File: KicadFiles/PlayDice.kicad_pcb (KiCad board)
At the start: 2 copper layers, 40 x 110 mm, 31 parts, among them J1 Clock In, J2 Eurorack_10_pin_power, J3 Action In, J4 OLED, J5 Gate Out, J6 CV Out, Q1 2N3904, Q2 2N3904, U1 LM1117-5.0, U3 TL072

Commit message: PCB fixed transistor connections; added basic handling for scale quantisation
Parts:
- Q1, Q2: value 2N3904 -> MMBT3904
- moved R4 7.02 mm to (131.0, 122.0), turned to 270 degrees
- moved Q2 5.59 mm to (137.5, 119.0)
- moved R3 3.04 mm to (135.0, 123.5)
- moved Q1 1.58 mm to (116.0, 145.5), turned to 180 degrees
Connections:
- Q1 pad 1: GND -> Net-(Q1-Pad1)
- Q1 pad 2: Net-(Q1-Pad2) -> GND
- Q2 pad 1: GND -> Net-(Q2-Pad1)
- Q2 pad 2: Net-(Q2-Pad2) -> GND
- R1 pad 1: Net-(Q1-Pad2) -> Net-(Q1-Pad1)
- R2 pad 1: Net-(Q1-Pad2) -> Net-(Q1-Pad1)
- R3 pad 1: Net-(Q2-Pad2) -> Net-(Q2-Pad1)
- R4 pad 1: Net-(Q2-Pad2) -> Net-(Q2-Pad1)
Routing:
- net Net-(Q1-Pad2): track 18.1 -> 0.00 mm
- net Net-(Q1-Pad1): track 0.00 -> 17.5 mm
- net Net-(Q2-Pad1): track 0.00 -> 9.81 mm
- net Net-(Q2-Pad2): track 5.59 -> 0.00 mm
- net /ACTIONCV: track 54.8 -> 51.5 mm
- net Net-(J3-Pad3): track 5.39 -> 3.22 mm
- net /CLOCK: track 84.5 -> 83.7 mm
- net (no net): track 0.00 -> 0.50 mm

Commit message: Bug Fixes and panel updates
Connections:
- Action1 pad 1: GND -> (no net)
- Action1 pad 3: (no net) -> GND
- Lane1 pad 1: GND -> (no net)
- Lane1 pad 3: (no net) -> GND
- Left1 pad 1: GND -> (no net)
- Left1 pad 3: (no net) -> GND
- Right1 pad 1: GND -> (no net)
- Right1 pad 3: (no net) -> GND
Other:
- board text added: "CV Out"
- board text added: "Clock In"
- board text added: "Gate Out"
- board text added: "Play Dice v 0.3"
- board text added: "RED -12"
- board text removed: "-12"
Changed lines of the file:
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@@
     (area 102.924999 48.924999 143.075001 159.075001)
     (thickness 1.6)
-    (drawings 7)
+    (drawings 14)
     (tracks 184)
     (zones 0)
@@
     (44 Edge.Cuts user)
     (45 Margin user)
-    (46 B.CrtYd user)
+    (46 B.CrtYd user hide)
     (47 F.CrtYd user)
-    (48 B.Fab user)
-    (49 F.Fab user)
+    (48 B.Fab user hide)
+    (49 F.Fab user hide)
   )
   (setup
@@
     (descr http://www.farnell.com/datasheets/1520732.pdf)
     (tags "connector multicomp MC9A MC9A12")
-    (fp_text reference J2 (at -3 -7 90) (layer F.SilkS) hide
+    (fp_text reference J2 (at 5 -7 90) (layer F.SilkS) hide
       (effects (font (size 1 1) (thickness 0.15)))
     )
@@
     (fp_line (start 8.8 -0.8) (end 8.8 -10.8) (layer B.Fab) (width 0.1))
     (fp_line (start 8.8 -10.8) (end -1.2 -10.8) (layer B.Fab) (width 0.1))
-    (pad 3 thru_hole circle (at 7.6 0 270) (size 1.8 1.8) (drill 0.9) (layers *.Cu *.Mask))
+    (pad 3 thru_hole circle (at 7.6 0 270) (size 1.8 1.8) (drill 0.9) (layers *.Cu *.Mask)
+      (net 2 GND))
     (pad 4 thru_hole circle (at 7.6 -11.6 270) (size 1.8 1.8) (drill 0.9) (layers *.Cu *.Mask))
-    (pad 1 thru_hole rect (at 0 0 270) (size 1.8 1.8) (drill 0.9) (layers *.Cu *.Mask)
-      (net 2 GND))
+    (pad 1 thru_hole rect (at 0 0 270) (size 1.8 1.8) (drill 0.9) (layers *.Cu *.Mask))
     (pad 2 thru_hole circle (at 0 -11.6 270) (size 1.8 1.8) (drill 0.9) (layers *.Cu *.Mask)
       (net 3 /ACTION))
@@
     (fp_line (start 8.8 -0.8) (end 8.8 -10.8) (layer B.Fab) (width 0.1))
     (fp_line (start 8.8 -10.8) (end -1.2 -10.8) (layer B.Fab) (width 0.1))
-    (pad 3 thru_hole circle (at 7.6 0 270) (size 1.8 1.8) (drill 0.9) (layers *.Cu *.Mask))
+    (pad 3 thru_hole circle (at 7.6 0 270) (size 1.8 1.8) (drill 0.9) (layers *.Cu *.Mask)
+      (net 2 GND))
     (pad 4 thru_hole circle (at 7.6 -11.6 270) (size 1.8 1.8) (drill 0.9) (layers *.Cu *.Mask))
-    (pad 1 thru_hole rect (at 0 0 270) (size 1.8 1.8) (drill 0.9) (layers *.Cu *.Mask)
-      (net 2 GND))
+    (pad 1 thru_hole rect (at 0 0 270) (size 1.8 1.8) (drill 0.9) (layers *.Cu *.Mask))
     (pad 2 thru_hole circle (at 0 -11.6 270) (size 1.8 1.8) (drill 0.9) (layers *.Cu *.Mask)
       (net 32 /LANE))
@@
     (fp_line (start 8.8 -0.8) (end 8.8 -10.8) (layer B.Fab) (width 0.1))
     (fp_line (start 8.8 -10.8) (end -1.2 -10.8) (layer B.Fab) (width 0.1))
-    (pad 3 thru_hole circle (at 7.6 0 270) (size 1.8 1.8) (drill 0.9) (layers *.Cu *.Mask))
+    (pad 3 thru_hole circle (at 7.6 0 270) (size 1.8 1.8) (drill 0.9) (layers *.Cu *.Mask)
+      (net 2 GND))
     (pad 4 thru_hole circle (at 7.6 -11.6 270) (size 1.8 1.8) (drill 0.9) (layers *.Cu *.Mask))
-    (pad 1 thru_hole rect (at 0 0 270) (size 1.8 1.8) (drill 0.9) (layers *.Cu *.Mask)
-      (net 2 GND))
+    (pad 1 thru_hole rect (at 0 0 270) (size 1.8 1.8) (drill 0.9) (layers *.Cu *.Mask))
     (pad 2 thru_hole circle (at 0 -11.6 270) (size 1.8 1.8) (drill 0.9) (layers *.Cu *.Mask)
       (net 33 /RIGHT))
@@
     (fp_line (start 8.8 -0.8) (end 8.8 -10.8) (layer B.Fab) (width 0.1))
     (fp_line (start 8.8 -10.8) (end -1.2 -10.8) (layer B.Fab) (width 0.1))
-    (pad 3 thru_hole circle (at 7.6 0 270) (size 1.8 1.8) (drill 0.9) (layers *.Cu *.Mask))
+    (pad 3 thru_hole circle (at 7.6 0 270) (size 1.8 1.8) (drill 0.9) (layers *.Cu *.Mask)
+      (net 2 GND))
     (pad 4 thru_hole circle (at 7.6 -11.6 270) (size 1.8 1.8) (drill 0.9) (layers *.Cu *.Mask))
-    (pad 1 thru_hole rect (at 0 0 270) (size 1.8 1.8) (drill 0.9) (layers *.Cu *.Mask)
-      (net 2 GND))
+    (pad 1 thru_hole rect (at 0 0 270) (size 1.8 1.8) (drill 0.9) (layers *.Cu *.Mask))
     (pad 2 thru_hole circle (at 0 -11.6 270) (size 1.8 1.8) (drill 0.9) (layers *.Cu *.Mask)
       (net 34 /LEFT))
@@
     (tags "resistor 0805")
     (attr smd)
-    (fp_text reference R7 (at -2.5 -2 180) (layer F.SilkS)
+    (fp_text reference R7 (at -1.5 -1.5 270) (layer F.SilkS)
       (effects (font (size 1 1) (thickness 0.15)))
     )
@@
     (tags "capacitor 0805")
     (attr smd)
-    (fp_text reference C4 (at -2.5 2 180) (layer F.SilkS)
+    (fp_text reference C4 (at 0 1.5 270) (layer F.SilkS)
       (effects (font (size 1 1) (thickness 0.15)))
     )
@@
     (pad "" np_thru_hole circle (at 0 0 180) (size 2.5 2.5) (drill 2.5) (layers *.Cu *.Mask))
   )
+  (gr_text "CV Out" (at 110 147.5) (layer F.SilkS)
+    (effects (font (size 1 1) (thickness 0.1)))
+  )
+  (gr_text "Gate Out" (at 123 147.5) (layer F.SilkS)
+    (effects (font (size 1 1) (thickness 0.1)))
+  )
+  (gr_text "Clock In" (at 136 147.5) (layer F.SilkS)
+    (effects (font (size 1 1) (thickness 0.1)))
+  )
+  (gr_line (start 120.5 113.25) (end 125.5 113.25) (angle 90) (layer F.SilkS) (width 0.2))
+  (gr_line (start 123 118.5) (end 123 117.5) (angle 90) (layer F.SilkS) (width 0.2))
+  (gr_line (start 123 113.5) (end 123 118) (angle 90) (layer F.SilkS) (width 0.2))
+  (gr_text "Play Dice\nv 0.3" (at 109 52.5) (layer F.SilkS)
+    (effects (font (size 1.2 1.2) (thickness 0.3)))
+  )
   (gr_circle (center 117 115) (end 117.5 115) (layer F.SilkS) (width 0.2))
   (gr_text +12 (at 122.5 122.5) (layer F.SilkS)
     (effects (font (size 1 1) (thickness 0.15)))
   )
-  (gr_text -12 (at 121.5 137.5) (layer F.SilkS)
+  (gr_text "RED\n-12" (at 129.5 135) (layer F.SilkS)
     (effects (font (size 1 1) (thickness 0.15)))
   )

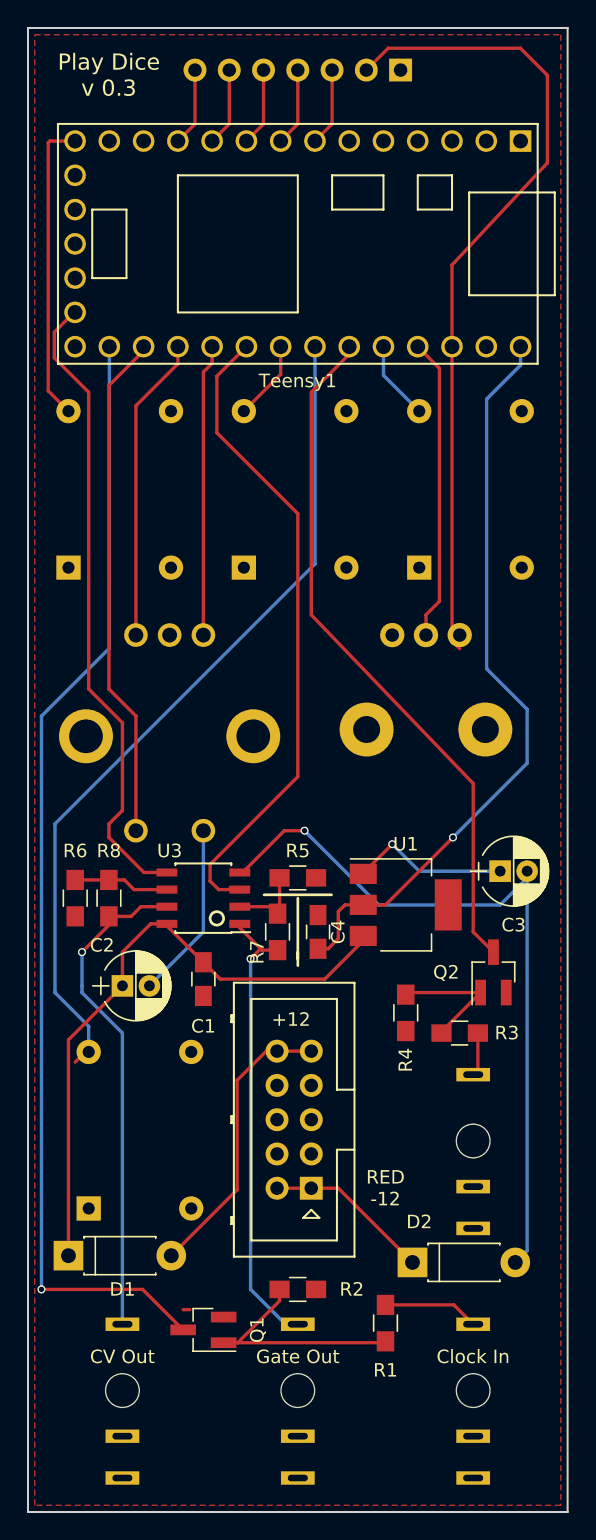
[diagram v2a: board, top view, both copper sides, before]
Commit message: Various code tidy-ups. Added configuration option for encoder direction. ADded new panel gerbers
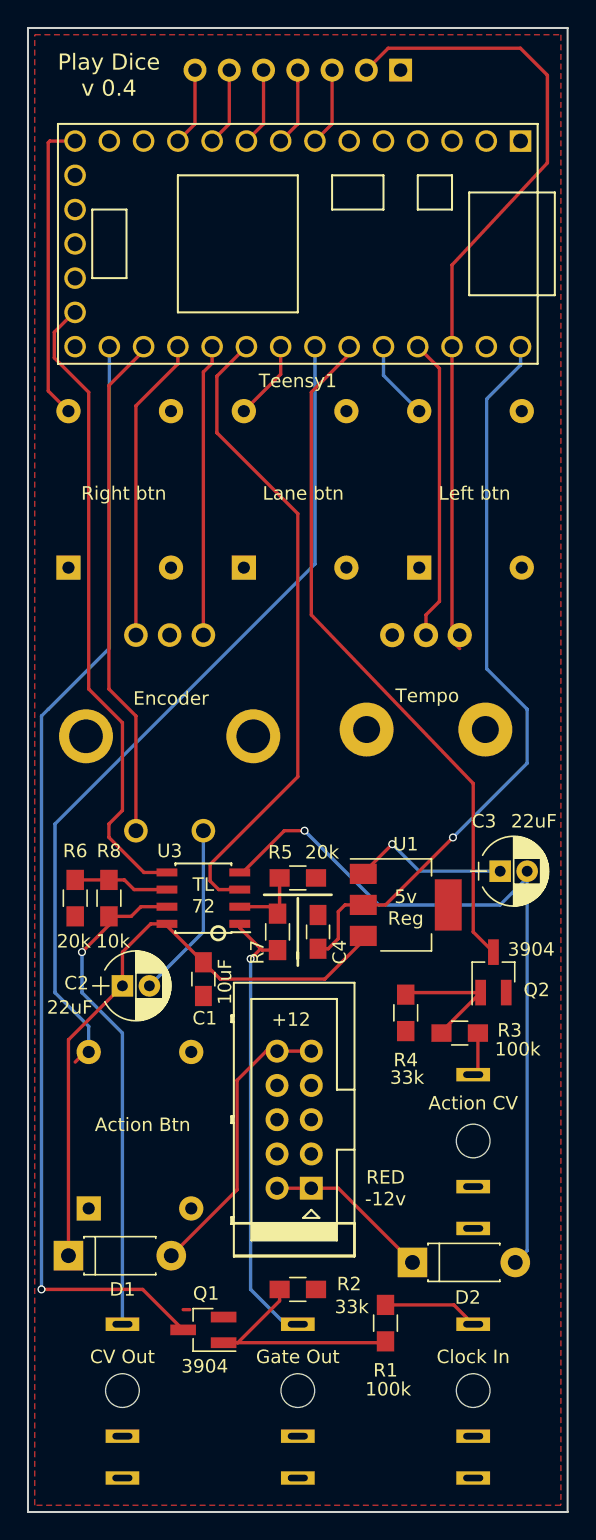
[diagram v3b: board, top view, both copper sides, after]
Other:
- board text added: "100k"
- board text added: "10k"
- board text added: "10uF"
- board text added: "20k"
- board text added: "22uF"
- board text added: "33k"
- board text added: "3904"
- board text added: "5v Reg"
- board text added: "Action Btn"
- board text added: "Action CV"
- board text added: "Encoder"
- board text added: "Lane btn"
- board text added: "Left btn"
- board text added: "Play Dice v 0.4"
- board text added: "RED -12v"
- board text added: "Right btn"
- board text added: "TL 72"
- board text added: "Tempo"
- board text removed: "Play Dice v 0.3"
- board text removed: "RED -12"
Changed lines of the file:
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@@
     (links 75)
     (no_connects 0)
-    (area 102.924999 48.924999 143.075001 159.075001)
+    (area 102.924999 44.05 143.075001 159.075001)
     (thickness 1.6)
-    (drawings 14)
+    (drawings 38)
     (tracks 184)
     (zones 0)
@@
       (drillshape 0)
       (scaleselection 1)
-      (outputdirectory Gerbers/))
+      (outputdirectory "Board Gerbers/"))
   )
   (net 0 "")
@@
     (descr "D, DO-41_SOD81 series, Axial, Horizontal, pin pitch=7.62mm, , length*diameter=5.2*2.7mm^2, , http://www.diodes.com/_files/packages/DO-41%20(Plastic).pdf")
     (tags "D DO-41_SOD81 series Axial Horizontal pin pitch 7.62mm  length 5.2mm diameter 2.7mm")
-    (fp_text reference D2 (at 0.5 -3) (layer F.SilkS)
+    (fp_text reference D2 (at 4.1 2.6) (layer F.SilkS)
       (effects (font (size 1 1) (thickness 0.15)))
     )
@@
     (descr "CP, Radial series, Radial, pin pitch=2.00mm, , diameter=5mm, Electrolytic Capacitor")
     (tags "CP Radial series Radial pin pitch 2.00mm  diameter 5mm Electrolytic Capacitor")
-    (fp_text reference C3 (at 1 4) (layer F.SilkS)
+    (fp_text reference C3 (at -1.2 -3.7) (layer F.SilkS)
       (effects (font (size 1 1) (thickness 0.15)))
     )
@@
     (descr "CP, Radial series, Radial, pin pitch=2.00mm, , diameter=5mm, Electrolytic Capacitor")
     (tags "CP Radial series Radial pin pitch 2.00mm  diameter 5mm Electrolytic Capacitor")
-    (fp_text reference C2 (at -1.5 -3 180) (layer F.SilkS)
+    (fp_text reference C2 (at -3.4 -0.2 180) (layer F.SilkS)
       (effects (font (size 1 1) (thickness 0.15)))
     )
@@
     (tags "resistor 0805")
     (attr smd)
-    (fp_text reference R2 (at 4 0) (layer F.SilkS)
+    (fp_text reference R2 (at 3.8 -0.4) (layer F.SilkS)
       (effects (font (size 1 1) (thickness 0.15)))
     )
@@
     (tags "resistor 0805")
     (attr smd)
-    (fp_text reference R3 (at 3.5 0) (layer F.SilkS)
+    (fp_text reference R3 (at 3.7 -0.2) (layer F.SilkS)
       (effects (font (size 1 1) (thickness 0.15)))
     )
@@
     (tags "resistor 0805")
     (attr smd)
-    (fp_text reference R4 (at 3.5 0 270) (layer F.SilkS)
+    (fp_text reference R4 (at 3.5 0 360) (layer F.SilkS)
       (effects (font (size 1 1) (thickness 0.15)))
     )
@@
     (tags "resistor 0805")
     (attr smd)
-    (fp_text reference R5 (at 0 2 180) (layer F.SilkS)
+    (fp_text reference R5 (at 1.3 1.9 180) (layer F.SilkS)
       (effects (font (size 1 1) (thickness 0.15)))
     )
@@
     (tags SOT-23)
     (attr smd)
-    (fp_text reference Q1 (at -4 0 270) (layer F.SilkS)
+    (fp_text reference Q1 (at -0.2 2.7 180) (layer F.SilkS)
       (effects (font (size 1 1) (thickness 0.15)))
     )
@@
     (tags SOT-23)
     (attr smd)
-    (fp_text reference Q2 (at 0 -3.5 180) (layer F.SilkS)
+    (fp_text reference Q2 (at -1.3 3.2 180) (layer F.SilkS)
       (effects (font (size 1 1) (thickness 0.15)))
     )
@@
     (tags "capacitor 0805")
     (attr smd)
-    (fp_text reference C1 (at 3.5 0 360) (layer F.SilkS)
+    (fp_text reference C1 (at 2.9 -0.1 360) (layer F.SilkS)
       (effects (font (size 1 1) (thickness 0.15)))
     )
@@
     (tags "capacitor 0805")
     (attr smd)
-    (fp_text reference C4 (at 0 1.5 270) (layer F.SilkS)
+    (fp_text reference C4 (at -1.5 1.6 270) (layer F.SilkS)
       (effects (font (size 1 1) (thickness 0.15)))
     )
@@
     (pad "" np_thru_hole circle (at 0 0 180) (size 2.5 2.5) (drill 2.5) (layers *.Cu *.Mask))
   )
+  (gr_text 10uF (at 117.6 119.7 90) (layer F.SilkS)
+    (effects (font (size 1 1) (thickness 0.1)))
+  )
+  (gr_text 22uF (at 140.5 107.8) (layer F.SilkS)
+    (effects (font (size 1 1) (thickness 0.1)))
+  )
+  (gr_text 22uF (at 106.1 121.6) (layer F.SilkS)
+    (effects (font (size 1 1) (thickness 0.1)))
+  )
+  (gr_text 3904 (at 116.1 148.2) (layer F.SilkS)
+    (effects (font (size 1 1) (thickness 0.1)))
+  )
+  (gr_text 3904 (at 140.3 117.3) (layer F.SilkS)
+    (effects (font (size 1 1) (thickness 0.1)))
+  )
+  (gr_text "5v\nReg" (at 131 114.2) (layer F.SilkS)
+    (effects (font (size 1 1) (thickness 0.1)))
+  )
+  (gr_text "TL\n72" (at 116 113.3) (layer F.SilkS)
+    (effects (font (size 1 1) (thickness 0.1)))
+  )
+  (gr_text 10k (at 109.3 116.7) (layer F.SilkS)
+    (effects (font (size 1 1) (thickness 0.1)))
+  )
+  (gr_text 20k (at 106.4 116.7) (layer F.SilkS)
+    (effects (font (size 1 1) (thickness 0.1)))
+  )
+  (gr_text 20k (at 124.8 110.1) (layer F.SilkS)
+    (effects (font (size 1 1) (thickness 0.1)))
+  )
+  (gr_text 33k (at 127 143.8) (layer F.SilkS)
+    (effects (font (size 1 1) (thickness 0.1)))
+  )
+  (gr_text 33k (at 131.1 126.8) (layer F.SilkS)
+    (effects (font (size 1 1) (thickness 0.1)))
+  )
+  (gr_text 100k (at 139.3 124.7) (layer F.SilkS)
+    (effects (font (size 1 1) (thickness 0.1)))
+  )
+  (gr_text 100k (at 129.7 149.9) (layer F.SilkS)
+    (effects (font (size 1 1) (thickness 0.1)))
+  )
+  (gr_line (start 127.2 140) (end 118.3 140) (angle 90) (layer F.SilkS) (width 0.2))
+  (gr_line (start 127.2 137.6) (end 127.2 140) (angle 90) (layer F.SilkS) (width 0.2))
+  (gr_line (start 118.3 137.6) (end 127.2 137.6) (angle 90) (layer F.SilkS) (width 0.2))
+  (gr_text "Left btn" (at 136.1 83.5) (layer F.SilkS)
+    (effects (font (size 1 1) (thickness 0.1)))
+  )
+  (gr_text "Lane btn" (at 123.4 83.5) (layer F.SilkS)
+    (effects (font (size 1 1) (thickness 0.1)))
+  )
+  (gr_text "Right btn" (at 110.1 83.5) (layer F.SilkS)
+    (effects (font (size 1 1) (thickness 0.1)))
+  )
+  (gr_text Tempo (at 132.6 98.5) (layer F.SilkS)
+    (effects (font (size 1 1) (thickness 0.1)))
+  )
+  (gr_text Encoder (at 113.6 98.7) (layer F.SilkS)
+    (effects (font (size 1 1) (thickness 0.1)))
+  )
+  (gr_text "Action CV" (at 136 128.7) (layer F.SilkS)
+    (effects (font (size 1 1) (thickness 0.1)))
+  )
+  (gr_text "Action Btn" (at 111.5 130.3) (layer F.SilkS)
+    (effects (font (size 1 1) (thickness 0.1)))
+  )
   (gr_text "CV Out" (at 110 147.5) (layer F.SilkS)
     (effects (font (size 1 1) (thickness 0.1)))
@@
   (gr_line (start 123 118.5) (end 123 117.5) (angle 90) (layer F.SilkS) (width 0.2))
   (gr_line (start 123 113.5) (end 123 118) (angle 90) (layer F.SilkS) (width 0.2))
-  (gr_text "Play Dice\nv 0.3" (at 109 52.5) (layer F.SilkS)
+  (gr_text "Play Dice\nv 0.4" (at 109 52.5) (layer F.SilkS)
     (effects (font (size 1.2 1.2) (thickness 0.3)))
   )
-  (gr_circle (center 117 115) (end 117.5 115) (layer F.SilkS) (width 0.2))
+  (gr_circle (center 117.1 116.1) (end 117.6 116.1) (layer F.SilkS) (width 0.2))
   (gr_text +12 (at 122.5 122.5) (layer F.SilkS)
     (effects (font (size 1 1) (thickness 0.15)))
   )
-  (gr_text "RED\n-12" (at 129.5 135) (layer F.SilkS)
+  (gr_text "RED\n-12v" (at 129.5 135) (layer F.SilkS)
     (effects (font (size 1 1) (thickness 0.15)))
   )
@@
       )
     )
+  )
+  (zone (net 0) (net_name "") (layer F.SilkS) (hatch edge 0.508)
+    (connect_pads (clearance 0.508))
+    (min_thickness 0.254)
+    (fill yes (arc_segments 16) (thermal_gap 0.508) (thermal_bridge_width 0.508))
+    (polygon
+      (pts
+        (xy 119.6 137.6) (xy 125.9 137.6) (xy 125.9 138.9) (xy 119.6 138.9)
+      )
+    )
